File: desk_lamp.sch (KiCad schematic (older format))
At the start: 31 parts, among them J1 CON-SOCJ-2155, J2 CON-SOCJ-2155, J3 Phoenix_Contact_1989764, Q1 2N7002K, Q2 MCB150N06YB-TP, U1 MCP1799T-3302H_DB, U2 MIC5365-1.2YC5-TR, U3 ECS-TXO-25CSMV-320-AM-TR, U4 ICE40LP384-SG32, U5 W25X10CLSNIG

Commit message: Fixed mosfet swapped pins
Gate and Drain pins were swapped.
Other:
- note added: "1.1 Alpha"
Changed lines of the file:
@@
 Wire Wire Line
 	8050 5800 7800 5800
+Text Notes 10600 7650 0    50   ~ 0
+1.1 Alpha
 $EndSCHEMATC

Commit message: Corrected TCXO and 3V3 LDO
TCXO was replaced with 25MHz that is no longer 0.8Vpp.

LDO did not match footprint. Replaced with compatible model that matched fabbed footprint.

Gerbers updated and could be sent to fab house if desired.
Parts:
- U1: value MCP1799T-3302H_DB -> MCP1703T-3302E/MB; symbol nezbyte:MCP1799T-3302H_DB -> nezbyte:MCP1703T-3302E_MB
- U3: value ECS-TXO-25CSMV-320-AM-TR -> ECS-TXO-2520-33-250-AN-TR; symbol nezbyte:ECS-TXO-25CSMV-320-AM-TR -> nezbyte:ECS-TXO-2520-33-250-AN-TR
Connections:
- net GND: no longer U3.1 (GND)
- no-connect marks 1 -> 2
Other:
- moved on the sheet: U3
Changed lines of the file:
@@
 	9750 4550 9750 4600
 $Comp
-L nezbyte:MCP1799T-3302H_DB U1
+L nezbyte:MCP1703T-3302E_MB U1
 U 1 1 5F603BDA
 P 1450 1450
 F 0 "U1" H 1650 1150 50  0000 C CNN
-F 1 "MCP1799T-3302H_DB" H 1450 1624 50  0000 C CNN
+F 1 "MCP1703T-3302E/MB" H 1450 1624 50  0000 C CNN
 F 2 "nezbyte:SOT-89-3" H 1450 1600 50  0001 C CNN
-F 3 "https://www.mouser.com/datasheet/2/268/MCP1799-Data-Sheet-20006248A-1658571.pdf" H 1450 1600 50  0001 C CNN
+F 3 "https://www.mouser.com/datasheet/2/268/22049a-51817.pdf" H 1450 1600 50  0001 C CNN
 	1    1450 1450
 	1    0    0    -1
@@
 SPI Flash\n
 $Comp
-L nezbyte:ECS-TXO-25CSMV-320-AM-TR U3
+L nezbyte:ECS-TXO-2520-33-250-AN-TR U3
 U 1 1 5F676A78
 P 5650 1550
 F 0 "U3" H 5420 1596 50  0000 R CNN
-F 1 "ECS-TXO-25CSMV-320-AM-TR" H 5420 1505 50  0000 R CNN
+F 1 "ECS-TXO-2520-33-250-AN-TR" H 5420 1505 50  0000 R CNN
 F 2 "nezbyte:Oscillator_SMD_ECS_2520MV-xxx-xx-4Pin_2.5x2.0mm" H 5750 2350 50  0001 C CNN
-F 3 "https://www.mouser.com/datasheet/2/122/ECS-TXO-25CSMV-1663914.pdf" H 5750 2350 50  0001 C CNN
+F 3 "https://www.mouser.com/datasheet/2/122/ECS_TXO_2520-1064138.pdf" H 5750 2350 50  0001 C CNN
 	1    5650 1550
 	1    0    0    -1
@@
 $EndComp
 Wire Wire Line
-	5550 1850 5650 1850
-Wire Wire Line
 	5650 1850 5650 1900
-Connection ~ 5650 1850
-Wire Wire Line
-	5650 1850 5750 1850
 Text GLabel 6050 1550 2    50   Input ~ 0
 CLK
@@
 Text Notes 10600 7650 0    50   ~ 0
 1.1 Alpha
+NoConn ~ 5350 1550
 $EndSCHEMATC

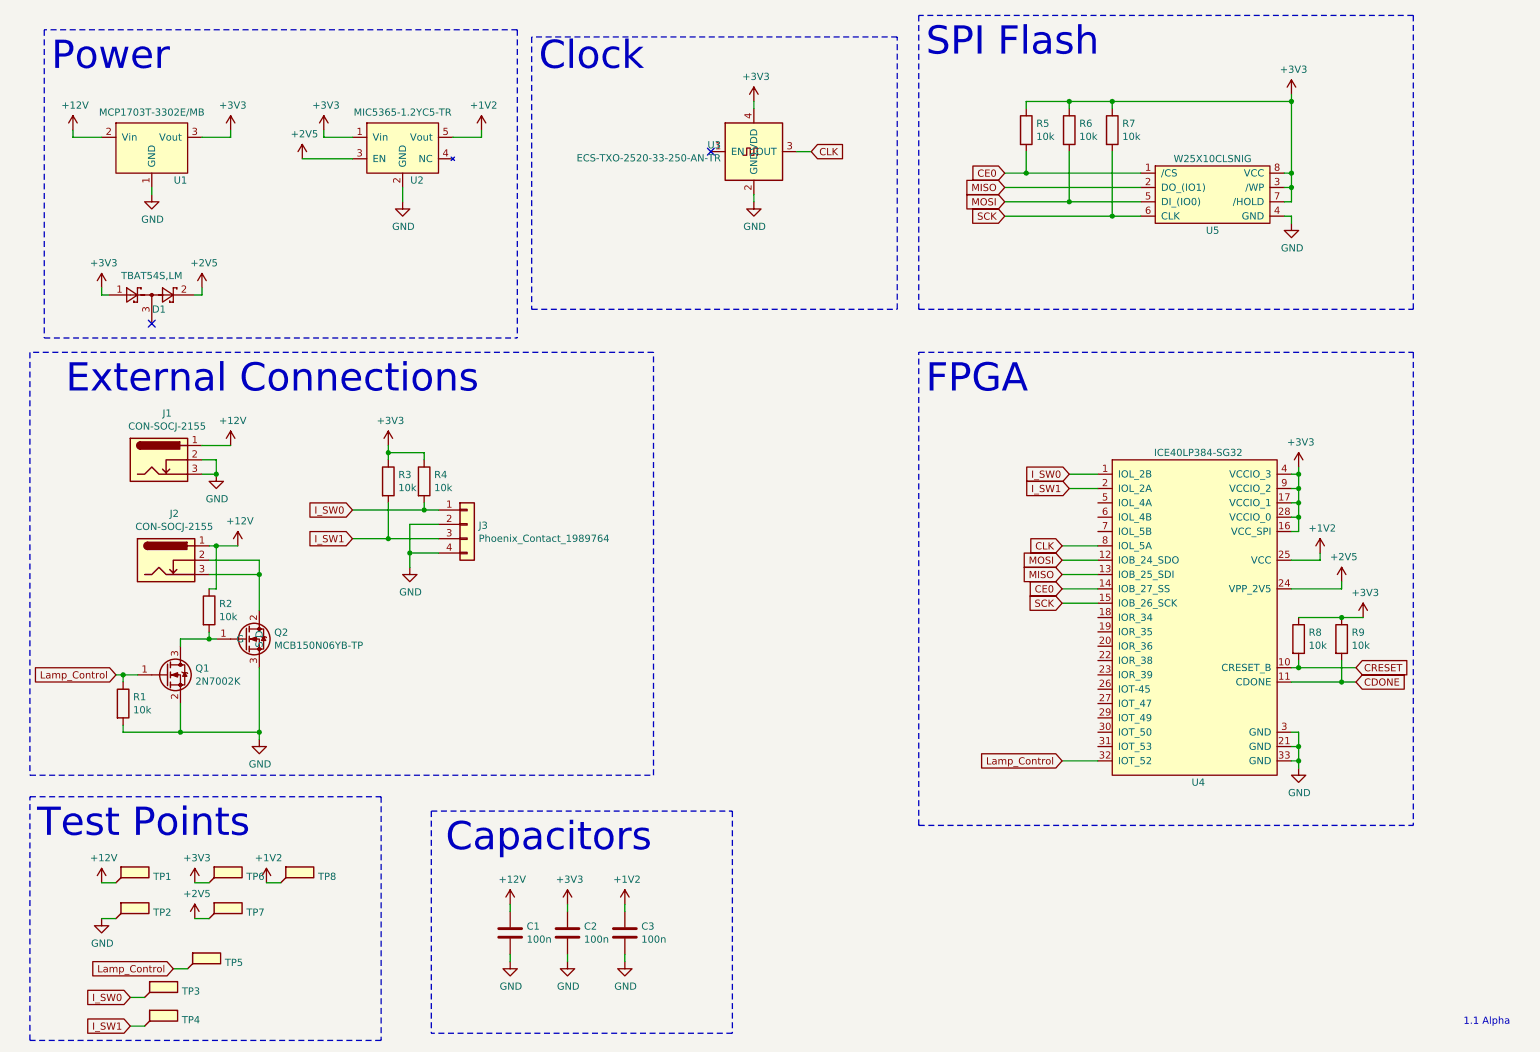
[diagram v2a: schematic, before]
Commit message: Switched to FPGA module
Switched to FPGA module to make changes easier going forward.
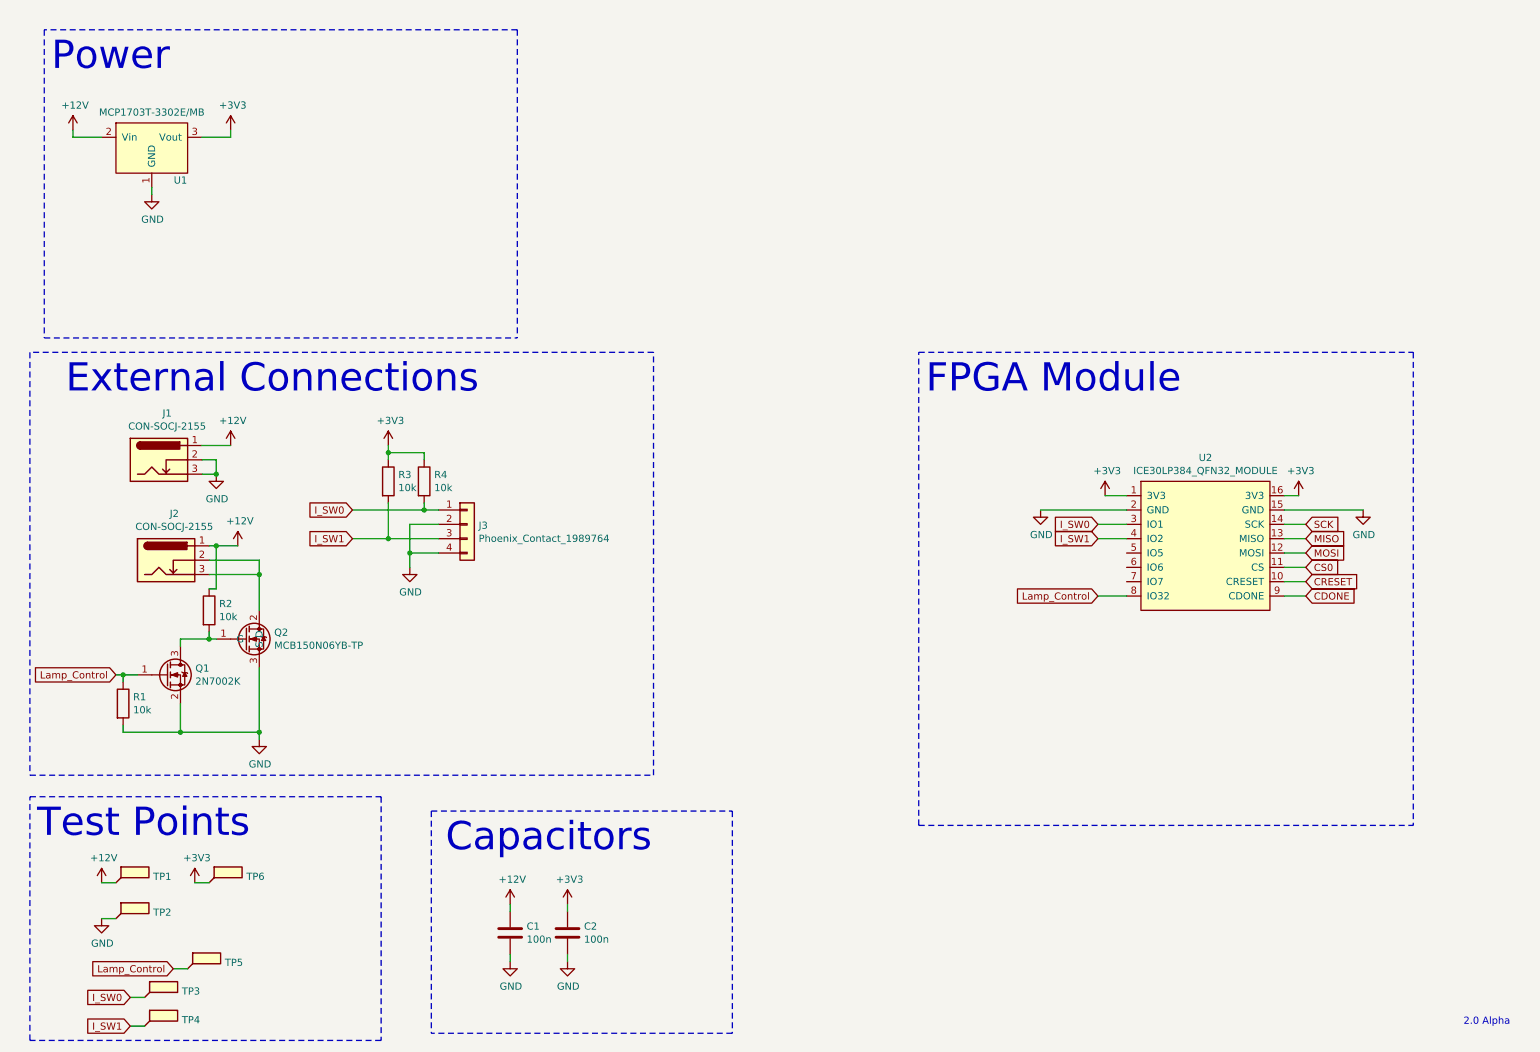
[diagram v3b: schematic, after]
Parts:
- removed C3: 100n, Capacitor_SMD:C_0805_2012Metric, symbol Device:C
- removed D1: TBAT54S,LM, nezbyte:SOT-23, symbol nezbyte:TBAT54S,LM
- removed R5, R6, R7, R8, R9: 10k, Resistor_SMD:R_0805_2012Metric, symbol Device:R
- removed TP7: 2.5V, nezbyte:TestPoint_5019, symbol nezbyte:TestPoint_5019
- removed TP8: 1.2V, nezbyte:TestPoint_5019, symbol nezbyte:TestPoint_5019
- removed U2: MIC5365-1.2YC5-TR, nezbyte:SOT-353_SC-70-5, symbol nezbyte:MIC5365-1.2YC5-TR
- removed U3: ECS-TXO-2520-33-250-AN-TR, nezbyte:Oscillator_SMD_ECS_2520MV-xxx-xx-4Pin_2.5x2.0mm, symbol nezbyte:ECS-TXO-2520-33-250-AN-TR
- removed U4: ICE40LP384-SG32, nezbyte:QFN-32-1EP_5x5mm_P0.5mm_EP3.1x3.1mm_ThermalVias, symbol nezbyte:ICE40LP384-SG32
- removed U5: W25X10CLSNIG, nezbyte:SOIC-8_3.9x4.9mm_P1.27mm, symbol nezbyte:W25X10CLSNIG
- added U2: ICE30LP384_QFN32_MODULE, nezbyte:ICE30LP384_QFN32_MODULE, symbol nezbyte:ICE30LP384_QFN32_MODULE
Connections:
- net +3V3: now also U2.1 (3V3), U2.16 (3V3)
- net CDONE: now also U2.9 (CDONE)
- net CRESET: now also U2.10 (CRESET)
- net GND: now also U2.15 (GND), U2.2 (GND)
- net I_SW0: now also U2.3 (IO1)
- net I_SW1: now also U2.4 (IO2)
- net Lamp_Control: now also U2.8 (IO32)
- net MISO: now also U2.13 (MISO)
- net MOSI: now also U2.12 (MOSI)
- net SCK: now also U2.14 (SCK)
- new net CS0: U2.11 (CS)
- no-connect marks 2 -> 0
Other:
- note added: "2.0 Alpha"
- note added: "FPGA Module\n"
- note removed: "1.1 Alpha"
- note removed: "Clock"
- note removed: "FPGA\n"
- note removed: "SPI Flash\n"
